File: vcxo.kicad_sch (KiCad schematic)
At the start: 27 parts, among them U901 DAC8551, U902 MCP1501-33xSN, U903 NCS325, U904 74LVC2GU04, U905 74LVC2G04, X901 DOT050V-020.0M

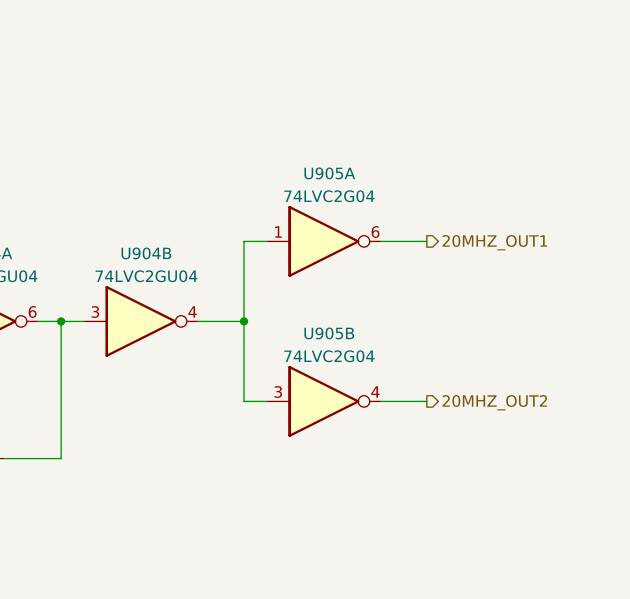
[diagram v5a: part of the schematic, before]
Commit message: VCXO, REF_IN: add reflection damping resistors
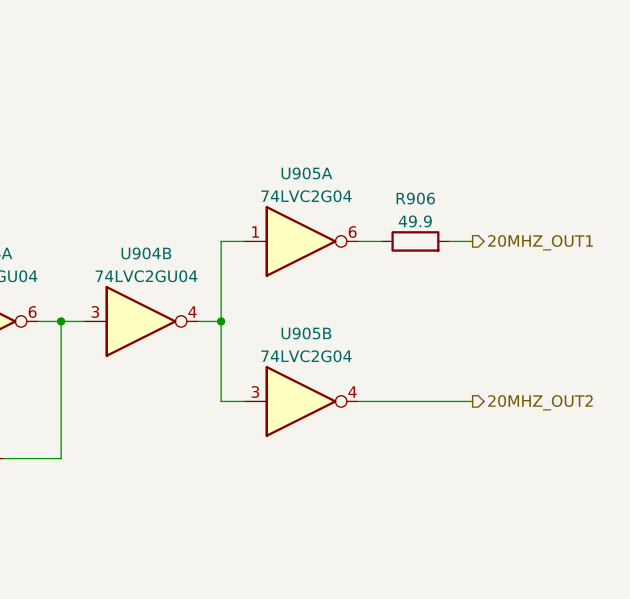
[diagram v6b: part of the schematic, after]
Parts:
- added R906: 49.9, Resistor_SMD:R_0805_2012Metric, symbol Device:R
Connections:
- net 20MHZ_OUT1: now also R906.2; no longer U905.6
- new net: R906.1, U905.6
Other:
- moved on the sheet: U905A, U905B
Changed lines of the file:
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@@
   (junction (at 82.55 127) (diameter 0) (color 0 0 0 0)
   )
-  (junction (at 240.03 118.11) (diameter 0) (color 0 0 0 0)
+  (junction (at 237.49 118.11) (diameter 0) (color 0 0 0 0)
   )
   (junction (at 88.9 26.67) (diameter 0) (color 0 0 0 0)
@@
     (stroke (width 0) (type default) (color 0 0 0 0))
   )
-  (wire (pts (xy 240.03 118.11) (xy 240.03 109.22))
+  (wire (pts (xy 237.49 118.11) (xy 237.49 109.22))
     (stroke (width 0) (type default) (color 0 0 0 0))
   )
@@
     (stroke (width 0) (type default) (color 0 0 0 0))
   )
-  (wire (pts (xy 234.95 118.11) (xy 240.03 118.11))
+  (wire (pts (xy 234.95 118.11) (xy 237.49 118.11))
     (stroke (width 0) (type default) (color 0 0 0 0))
   )
@@
     (stroke (width 0) (type default) (color 0 0 0 0))
   )
-  (wire (pts (xy 242.57 127) (xy 240.03 127))
+  (wire (pts (xy 240.03 127) (xy 237.49 127))
     (stroke (width 0) (type default) (color 0 0 0 0))
   )
@@
     (stroke (width 0) (type default) (color 0 0 0 0))
   )
+  (wire (pts (xy 262.89 109.22) (xy 265.43 109.22))
+    (stroke (width 0) (type default) (color 0 0 0 0))
+  )
   (bus (pts (xy 40.64 121.92) (xy 40.64 124.46))
     (stroke (width 0) (type default) (color 0 0 0 0))
@@
     (stroke (width 0) (type default) (color 0 0 0 0))
   )
-  (wire (pts (xy 240.03 127) (xy 240.03 118.11))
+  (wire (pts (xy 237.49 127) (xy 237.49 118.11))
     (stroke (width 0) (type default) (color 0 0 0 0))
   )
@@
     (stroke (width 0) (type default) (color 0 0 0 0))
   )
-  (wire (pts (xy 240.03 109.22) (xy 242.57 109.22))
+  (wire (pts (xy 237.49 109.22) (xy 240.03 109.22))
     (stroke (width 0) (type default) (color 0 0 0 0))
   )
@@
     (stroke (width 0) (type default) (color 0 0 0 0))
   )
-  (wire (pts (xy 255.27 127) (xy 260.35 127))
+  (wire (pts (xy 252.73 127) (xy 265.43 127))
     (stroke (width 0) (type default) (color 0 0 0 0))
   )
@@
     (stroke (width 0) (type default) (color 0 0 0 0))
   )
-  (wire (pts (xy 255.27 109.22) (xy 260.35 109.22))
+  (wire (pts (xy 252.73 109.22) (xy 255.27 109.22))
     (stroke (width 0) (type default) (color 0 0 0 0))
   )
@@
     (effects (font (size 1.27 1.27)) (justify left bottom))
   )
-  (hierarchical_label "20MHZ_OUT1" (shape output) (at 260.35 109.22 0)
+  (hierarchical_label "20MHZ_OUT1" (shape output) (at 265.43 109.22 0)
     (effects (font (size 1.27 1.27)) (justify left))
   )
@@
     (effects (font (size 1.27 1.27)) (justify right))
   )
-  (hierarchical_label "20MHZ_OUT2" (shape output) (at 260.35 127 0)
+  (hierarchical_label "20MHZ_OUT2" (shape output) (at 265.43 127 0)
     (effects (font (size 1.27 1.27)) (justify left))
   )
@@
     (pin "2")
   )
-  (symbol (lib_id "symbols:74LVC2G04") (at 247.65 109.22 0) (unit 1)
-    (in_bom yes) (on_board yes) (fields_autoplaced)
-    (property "Reference" "U905" (id 0) (at 249.4915 101.7102 0))
-    (property "Value" "74LVC2G04" (id 1) (at 249.4915 104.2471 0))
-    (property "Footprint" "Package_TO_SOT_SMD:SOT-23-6" (id 2) (at 247.65 91.44 0)
-      (effects (font (size 1.27 1.27)) hide)
-    )
-    (property "Datasheet" "https://assets.nexperia.com/documents/data-sheet/74LVC2GU04.pdf" (id 3) (at 246.38 88.9 0)
-      (effects (font (size 1.27 1.27)) hide)
-    )
-    (property "Mfr" "Nexperia" (id 4) (at 247.65 109.22 0)
-      (effects (font (size 1.27 1.27)) hide)
-    )
-    (property "Mfr PN" "74LVC2G04GV-Q100H" (id 5) (at 247.65 109.22 0)
+  (symbol (lib_id "symbols:74LVC2G04") (at 245.11 109.22 0) (unit 1)
+    (in_bom yes) (on_board yes) (fields_autoplaced)
+    (property "Reference" "U905" (id 0) (at 246.9515 101.7102 0))
+    (property "Value" "74LVC2G04" (id 1) (at 246.9515 104.2471 0))
+    (property "Footprint" "Package_TO_SOT_SMD:SOT-23-6" (id 2) (at 245.11 91.44 0)
+      (effects (font (size 1.27 1.27)) hide)
+    )
+    (property "Datasheet" "https://assets.nexperia.com/documents/data-sheet/74LVC2GU04.pdf" (id 3) (at 243.84 88.9 0)
+      (effects (font (size 1.27 1.27)) hide)
+    )
+    (property "Mfr" "Nexperia" (id 4) (at 245.11 109.22 0)
+      (effects (font (size 1.27 1.27)) hide)
+    )
+    (property "Mfr PN" "74LVC2G04GV-Q100H" (id 5) (at 245.11 109.22 0)
       (effects (font (size 1.27 1.27)) hide)
     )
@@
     )
     (property "Mfr PN" "CL21B104KBFNNNE" (id 8) (at 177.8 33.02 0)
+      (effects (font (size 1.27 1.27)) hide)
+    )
+    (pin "1")
+    (pin "2")
+  )
+  (symbol (lib_id "Device:R") (at 259.08 109.22 90) (unit 1)
+    (in_bom yes) (on_board yes) (fields_autoplaced)
+    (property "Reference" "R906" (id 0) (at 259.08 104.5042 90))
+    (property "Value" "49.9" (id 1) (at 259.08 107.0411 90))
+    (property "Footprint" "Resistor_SMD:R_0805_2012Metric" (id 2) (at 259.08 110.998 90)
+      (effects (font (size 1.27 1.27)) hide)
+    )
+    (property "Datasheet" "~" (id 3) (at 259.08 109.22 0)
+      (effects (font (size 1.27 1.27)) hide)
+    )
+    (property "Mfr" "Bourns" (id 4) (at 259.08 109.22 0)
+      (effects (font (size 1.27 1.27)) hide)
+    )
+    (property "Mfr PN" "CR0805-FX-49R9ELF" (id 5) (at 259.08 109.22 0)
       (effects (font (size 1.27 1.27)) hide)
     )
@@
     (pin "1")
   )
-  (symbol (lib_id "symbols:74LVC2G04") (at 247.65 127 0) (unit 2)
-    (in_bom yes) (on_board yes) (fields_autoplaced)
-    (property "Reference" "U905" (id 0) (at 249.4915 119.4902 0))
-    (property "Value" "74LVC2G04" (id 1) (at 249.4915 122.0271 0))
-    (property "Footprint" "Package_TO_SOT_SMD:SOT-23-6" (id 2) (at 247.65 109.22 0)
-      (effects (font (size 1.27 1.27)) hide)
-    )
-    (property "Datasheet" "https://assets.nexperia.com/documents/data-sheet/74LVC2GU04.pdf" (id 3) (at 246.38 106.68 0)
-      (effects (font (size 1.27 1.27)) hide)
-    )
-    (property "Mfr" "Nexperia" (id 4) (at 247.65 127 0)
-      (effects (font (size 1.27 1.27)) hide)
-    )
-    (property "Mfr PN" "74LVC2G04GV-Q100H" (id 5) (at 247.65 127 0)
-      (effects (font (size 1.27 1.27)) hide)
-    )
+  (symbol (lib_id "symbols:74LVC2G04") (at 245.11 127 0) (unit 2)
+    (in_bom yes) (on_board yes) (fields_autoplaced)
+    (property "Reference" "U905" (id 0) (at 246.9515 119.4902 0))
+    (property "Value" "74LVC2G04" (id 1) (at 246.9515 122.0271 0))
+    (property "Footprint" "Package_TO_SOT_SMD:SOT-23-6" (id 2) (at 245.11 109.22 0)
+      (effects (font (size 1.27 1.27)) hide)
+    )
+    (property "Datasheet" "https://assets.nexperia.com/documents/data-sheet/74LVC2GU04.pdf" (id 3) (at 243.84 106.68 0)
+      (effects (font (size 1.27 1.27)) hide)
+    )
+    (property "Mfr" "Nexperia" (id 4) (at 245.11 127 0)
+      (effects (font (size 1.27 1.27)) hide)
+    )
+    (property "Mfr PN" "74LVC2G04GV-Q100H" (id 5) (at 245.11 127 0)
+      (effects (font (size 1.27 1.27)) hide)
+    )

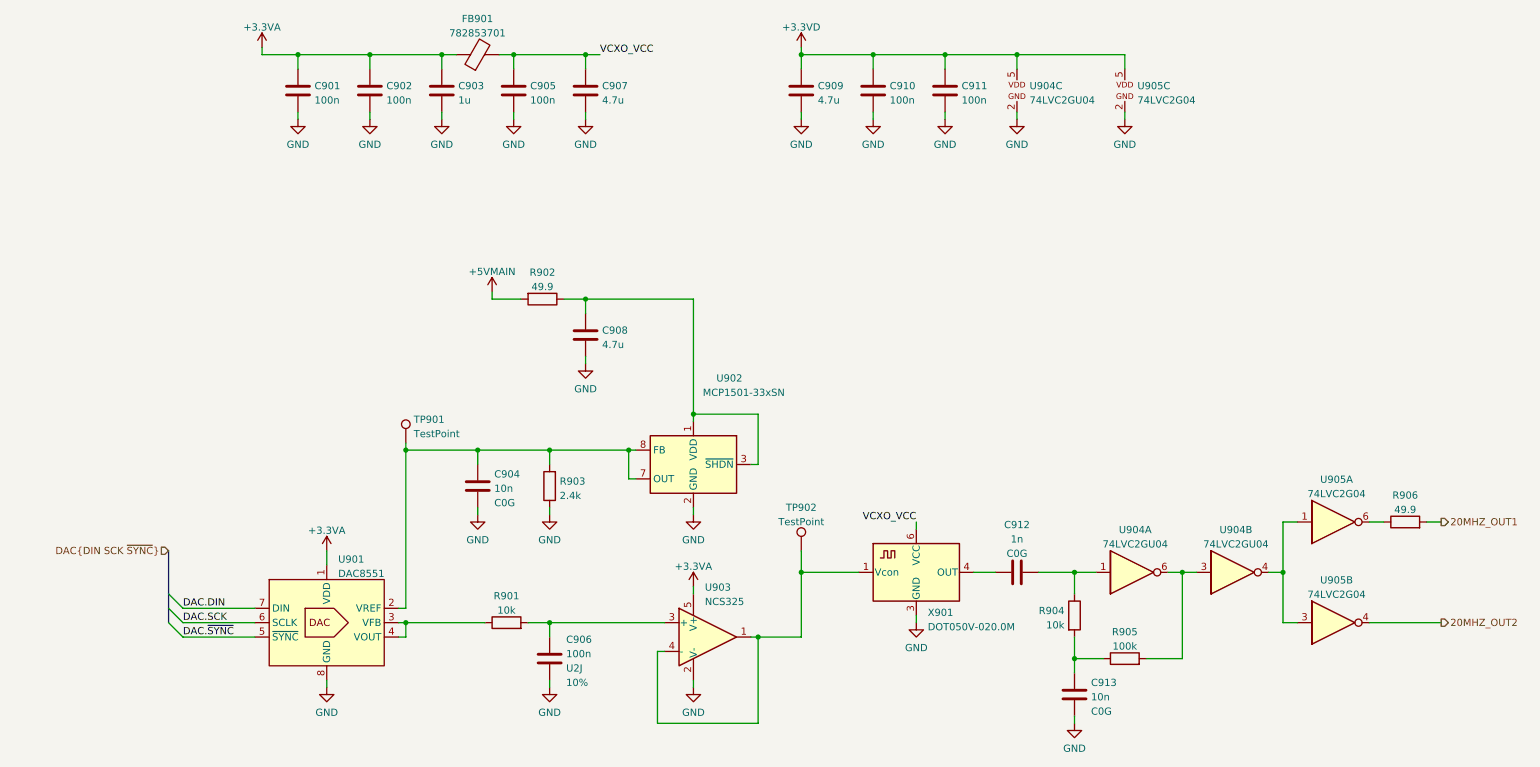
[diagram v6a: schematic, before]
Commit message: Update schematic: - Redesign of decoupling based on swcad modelling (predominantly use 1uf, no paralleled caps) - Reroute REF_CLK_IN, CLK_SEL net to different FPGA pins - Some net renaming - Ext conn: add decoupling to 3v3 output - Reassign references to all components PCB: routing almost finished
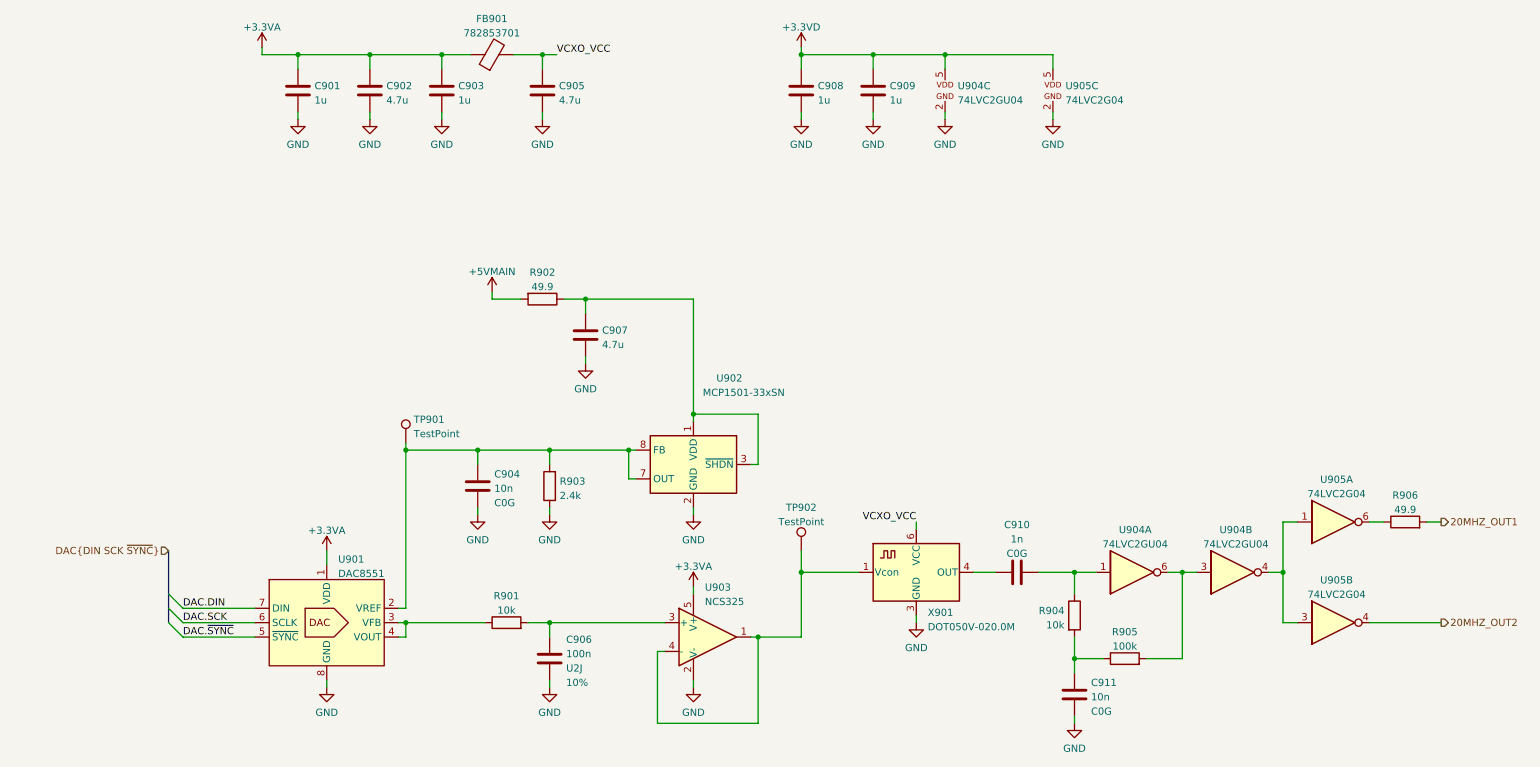
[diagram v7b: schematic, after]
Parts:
- removed C905, C910, C911: 100n, Capacitor_SMD:C_0805_2012Metric, symbol Device:C
- added C908: 1u, Capacitor_SMD:C_0805_2012Metric, symbol Device:C
- C901: value 100n -> 1u; Mfr PN CL21B104KBFNNNE -> CL21B105KOFNNNG
- C902: value 100n -> 4.7u; Mfr Samsung -> Murata; Mfr PN CL21B104KBFNNNE -> GRM21BR71C475ME51
- C909: value 4.7u -> 1u; Mfr Murata -> Samsung; Mfr PN GRM21BR71C475ME51 -> CL21B105KOFNNNG
- renumbered C907 to C905, C908 to C907, C912 to C910, C913 to C911
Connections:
- net +3.3VD: now also C908.2
- net GND: now also C908.1
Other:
- moved on the sheet: C905, FB901, U904C, U905C

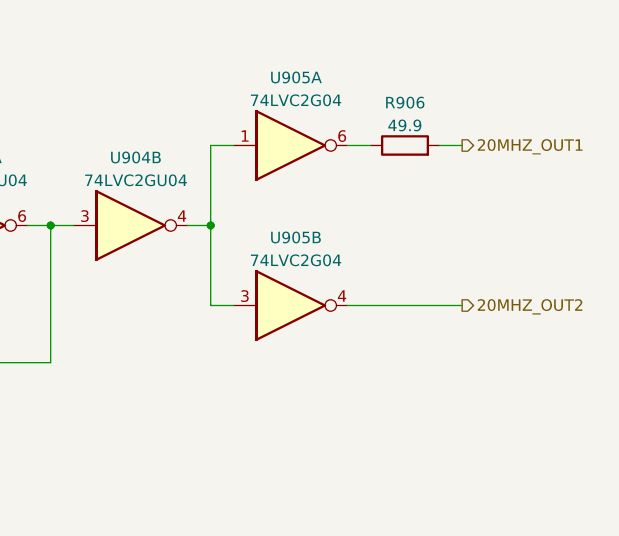
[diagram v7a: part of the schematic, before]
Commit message: - Add matching / anti-ring resistors to clock nets - Use 0603 resistors for anti-ring - Improve CLK_OUT routing
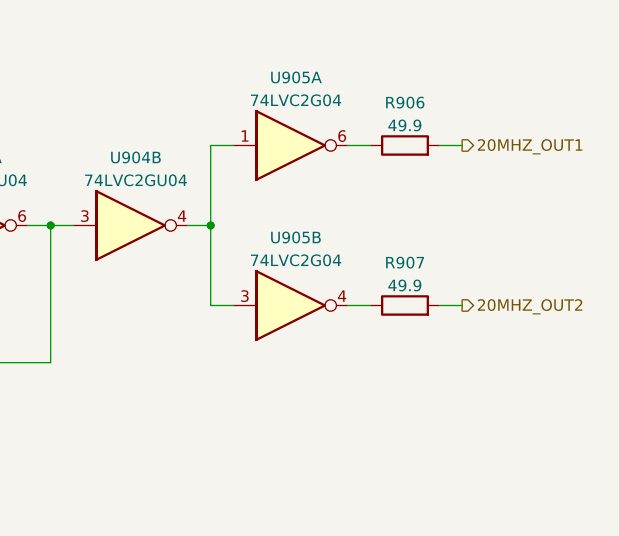
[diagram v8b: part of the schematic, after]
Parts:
- added R907: 49.9, Resistor_SMD:R_0603_1608Metric, symbol Device:R
- R906: footprint Resistor_SMD:R_0805_2012Metric -> Resistor_SMD:R_0603_1608Metric; Mfr PN CR0805-FX-49R9ELF -> CR0603-FX-49R9ELF
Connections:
- net 20MHZ_OUT2: now also R907.2; no longer U905.4
- new net: R907.1, U905.4
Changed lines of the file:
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@@
     (stroke (width 0) (type default) (color 0 0 0 0))
   )
-  (wire (pts (xy 252.73 127) (xy 265.43 127))
+  (wire (pts (xy 252.73 127) (xy 255.27 127))
     (stroke (width 0) (type default) (color 0 0 0 0))
   )
@@
   )
   (wire (pts (xy 213.36 133.35) (xy 219.71 133.35))
+    (stroke (width 0) (type default) (color 0 0 0 0))
+  )
+  (wire (pts (xy 262.89 127) (xy 265.43 127))
     (stroke (width 0) (type default) (color 0 0 0 0))
   )
@@
     (property "Reference" "R906" (id 0) (at 259.08 104.5042 90))
     (property "Value" "49.9" (id 1) (at 259.08 107.0411 90))
-    (property "Footprint" "Resistor_SMD:R_0805_2012Metric" (id 2) (at 259.08 110.998 90)
+    (property "Footprint" "Resistor_SMD:R_0603_1608Metric" (id 2) (at 259.08 110.998 90)
       (effects (font (size 1.27 1.27)) hide)
     )
@@
       (effects (font (size 1.27 1.27)) hide)
     )
-    (property "Mfr PN" "CR0805-FX-49R9ELF" (id 5) (at 259.08 109.22 0)
+    (property "Mfr PN" "CR0603-FX-49R9ELF" (id 5) (at 259.08 109.22 0)
       (effects (font (size 1.27 1.27)) hide)
     )
@@
     (pin "8")
   )
+  (symbol (lib_id "Device:R") (at 259.08 127 90) (unit 1)
+    (in_bom yes) (on_board yes) (fields_autoplaced)
+    (property "Reference" "R907" (id 0) (at 259.08 122.2842 90))
+    (property "Value" "49.9" (id 1) (at 259.08 124.8211 90))
+    (property "Footprint" "Resistor_SMD:R_0603_1608Metric" (id 2) (at 259.08 128.778 90)
+      (effects (font (size 1.27 1.27)) hide)
+    )
+    (property "Datasheet" "~" (id 3) (at 259.08 127 0)
+      (effects (font (size 1.27 1.27)) hide)
+    )
+    (property "Mfr" "Bourns" (id 4) (at 259.08 127 0)
+      (effects (font (size 1.27 1.27)) hide)
+    )
+    (property "Mfr PN" "CR0603-FX-49R9ELF" (id 5) (at 259.08 127 0)
+      (effects (font (size 1.27 1.27)) hide)
+    )
+    (pin "1")
+    (pin "2")
+  )
   (symbol (lib_id "Device:R") (at 200.66 125.73 0) (unit 1)
